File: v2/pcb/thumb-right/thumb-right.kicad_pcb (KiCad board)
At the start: 2 copper layers, 79.9 x 81.2 mm, 24 parts, among them J1 Conn_01x10, SW1 SW_SPDT, SW2 SW_Push, SW3 SW_Push, SW4 SW_Push, SW5 SW_Push, U1 xiao-ble, U2 PMW3610, U3 TLV70218_SOT23-5

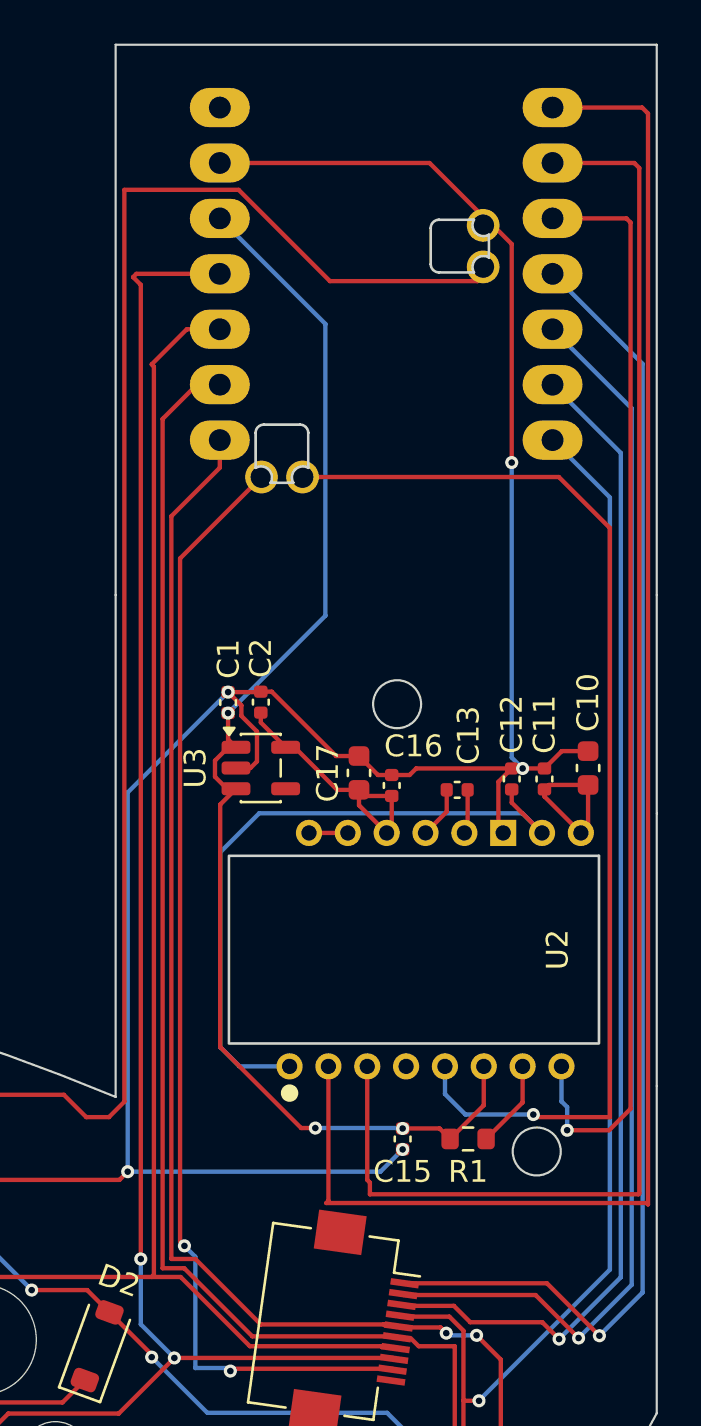
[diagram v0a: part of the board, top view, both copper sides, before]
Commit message: fix(pcb): offset the XIAO through-hole drills, re-sync the thumb boards
All 14 XIAO nRF52840 header pads in the shared mcu_roba footprint went
from a centred `drill 1` to `drill 0.8128` with `(offset ±0.5 0)`, i.e.
a 32-mil hole pushed toward the board edge inside the same 2.75x1.8 oval
pad. That leaves the inner half of the pad as exposed copper, so the
module can be reflowed/hand-soldered on its castellations instead of
only being pinned through. Pad centres also snap 7.625 -> 7.62.

Propagated into the two v2 thumb boards (the only boards carrying a
XIAO) via "update footprints from library", plus the handful of track
segments that had to move with the new hole positions.

Verified against the as-built files:
  * the thumb-board netlists are byte-identical to HEAD — every
    ROW/COL/SPI assignment is unchanged, so the firmware pin map still
    matches
  * the exported thumb gerbers carry the new tool (PTH T4C0.813)
  * NPTH tooling is still only 3.05/5.05 — the library update did NOT
    resurrect the Choc V2 fixing-leg holes on any of the 40 switches

Co-Authored-By: Claude Opus 5 (1M context) <noreply@anthropic.com>
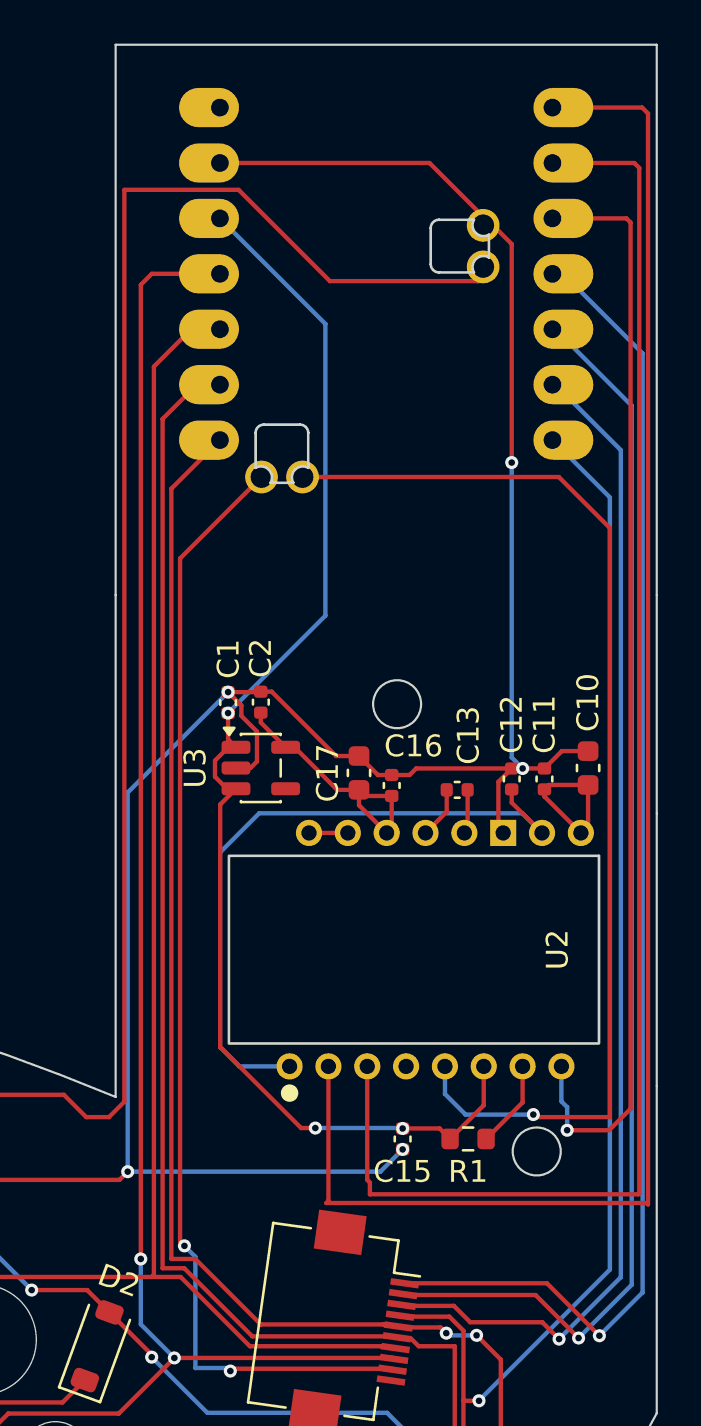
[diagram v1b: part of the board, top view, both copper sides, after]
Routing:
- net /COL2: track 77.0 -> 78.3 mm
- net /BAT_SW: track 85.4 -> 86.2 mm
- net /COL3: track 109.3 -> 108.6 mm
